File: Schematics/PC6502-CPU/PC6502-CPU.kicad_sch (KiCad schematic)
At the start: 62 parts, among them J1 BUS, J4 TEST, J5 Conn_02x05_Odd_Even, J6 Conn_02x02_Odd_Even, U2 AS6C4008-55PCN, U3 SST39SF010, U4 ATF1502AS, U5 W65C02, U6 74AHC244, U8 MCP130-450DI/TO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

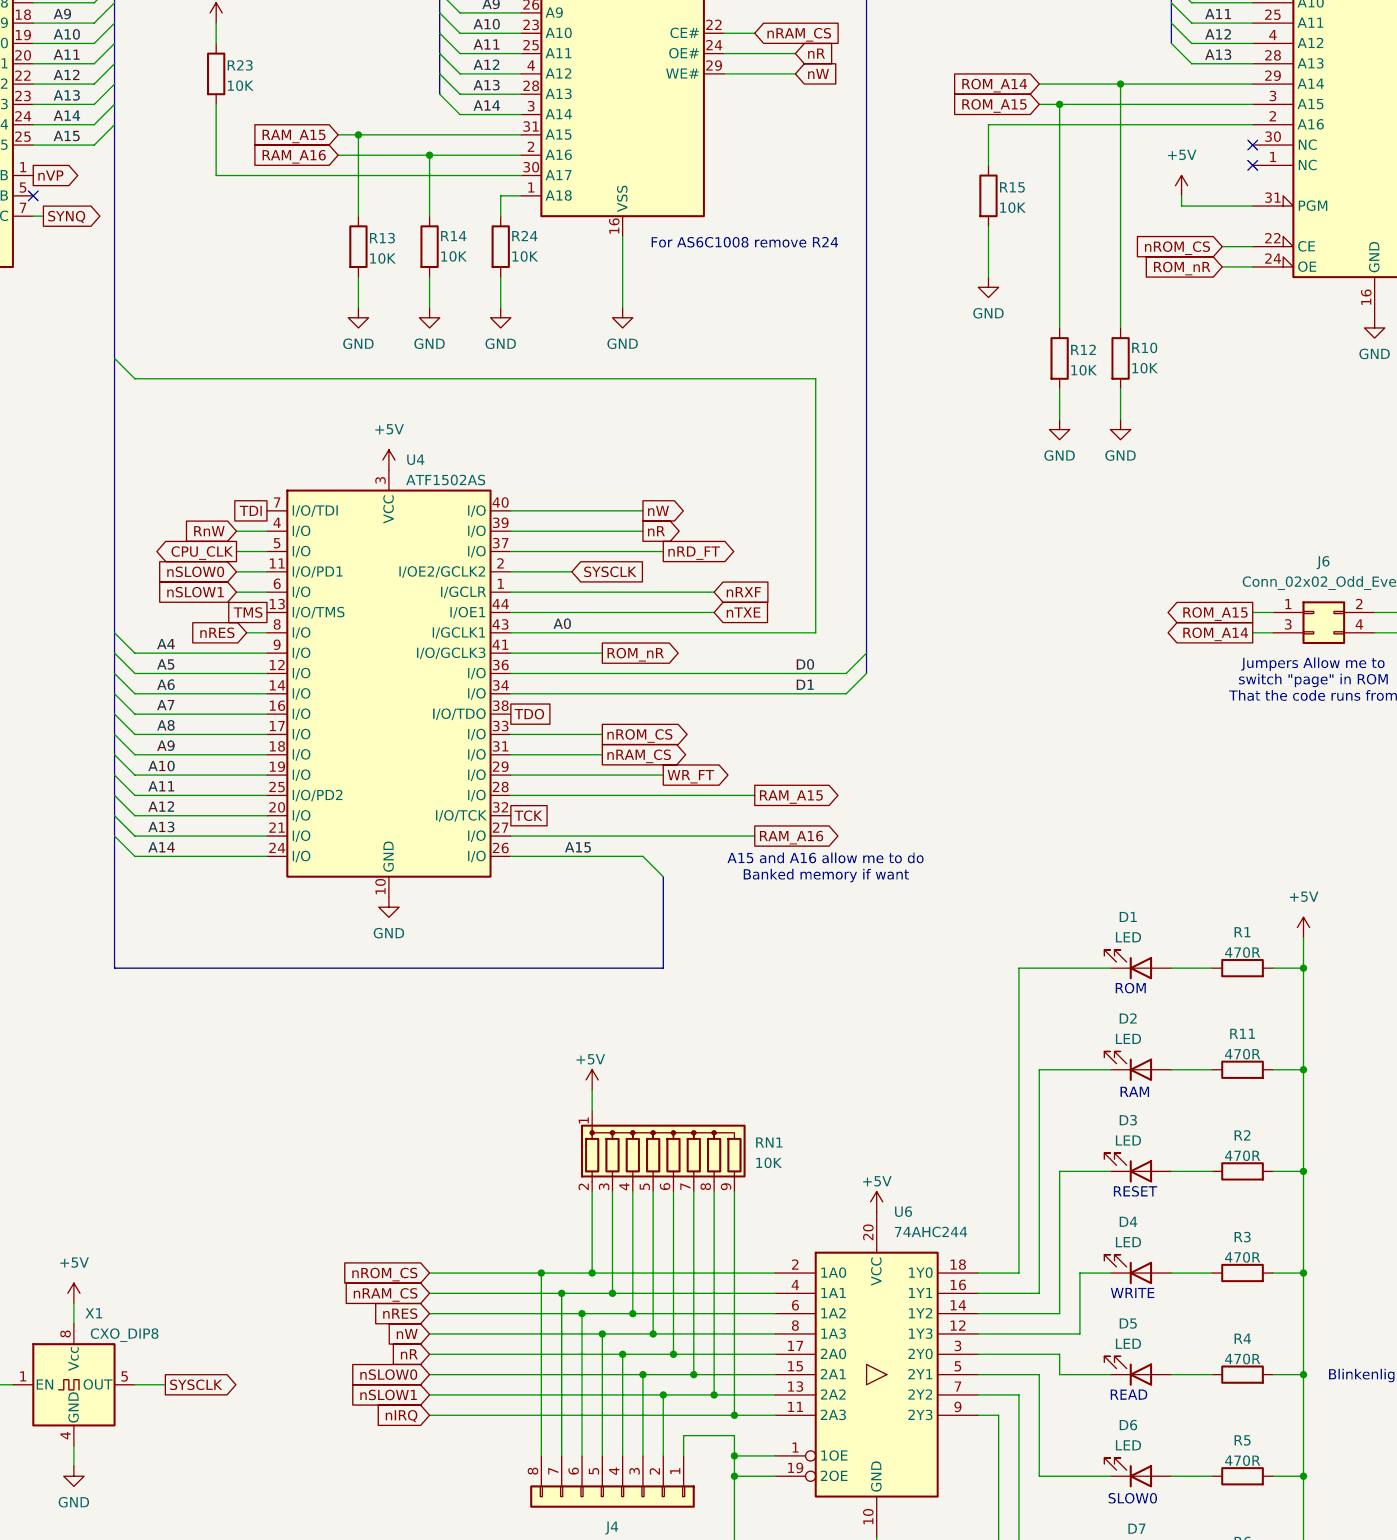
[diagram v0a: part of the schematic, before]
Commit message: Updated Schematics and CPLD files
Files updated for the CPU & FM Speech board
Also revised CPLDs for CPU, VIA and Compact Flasg
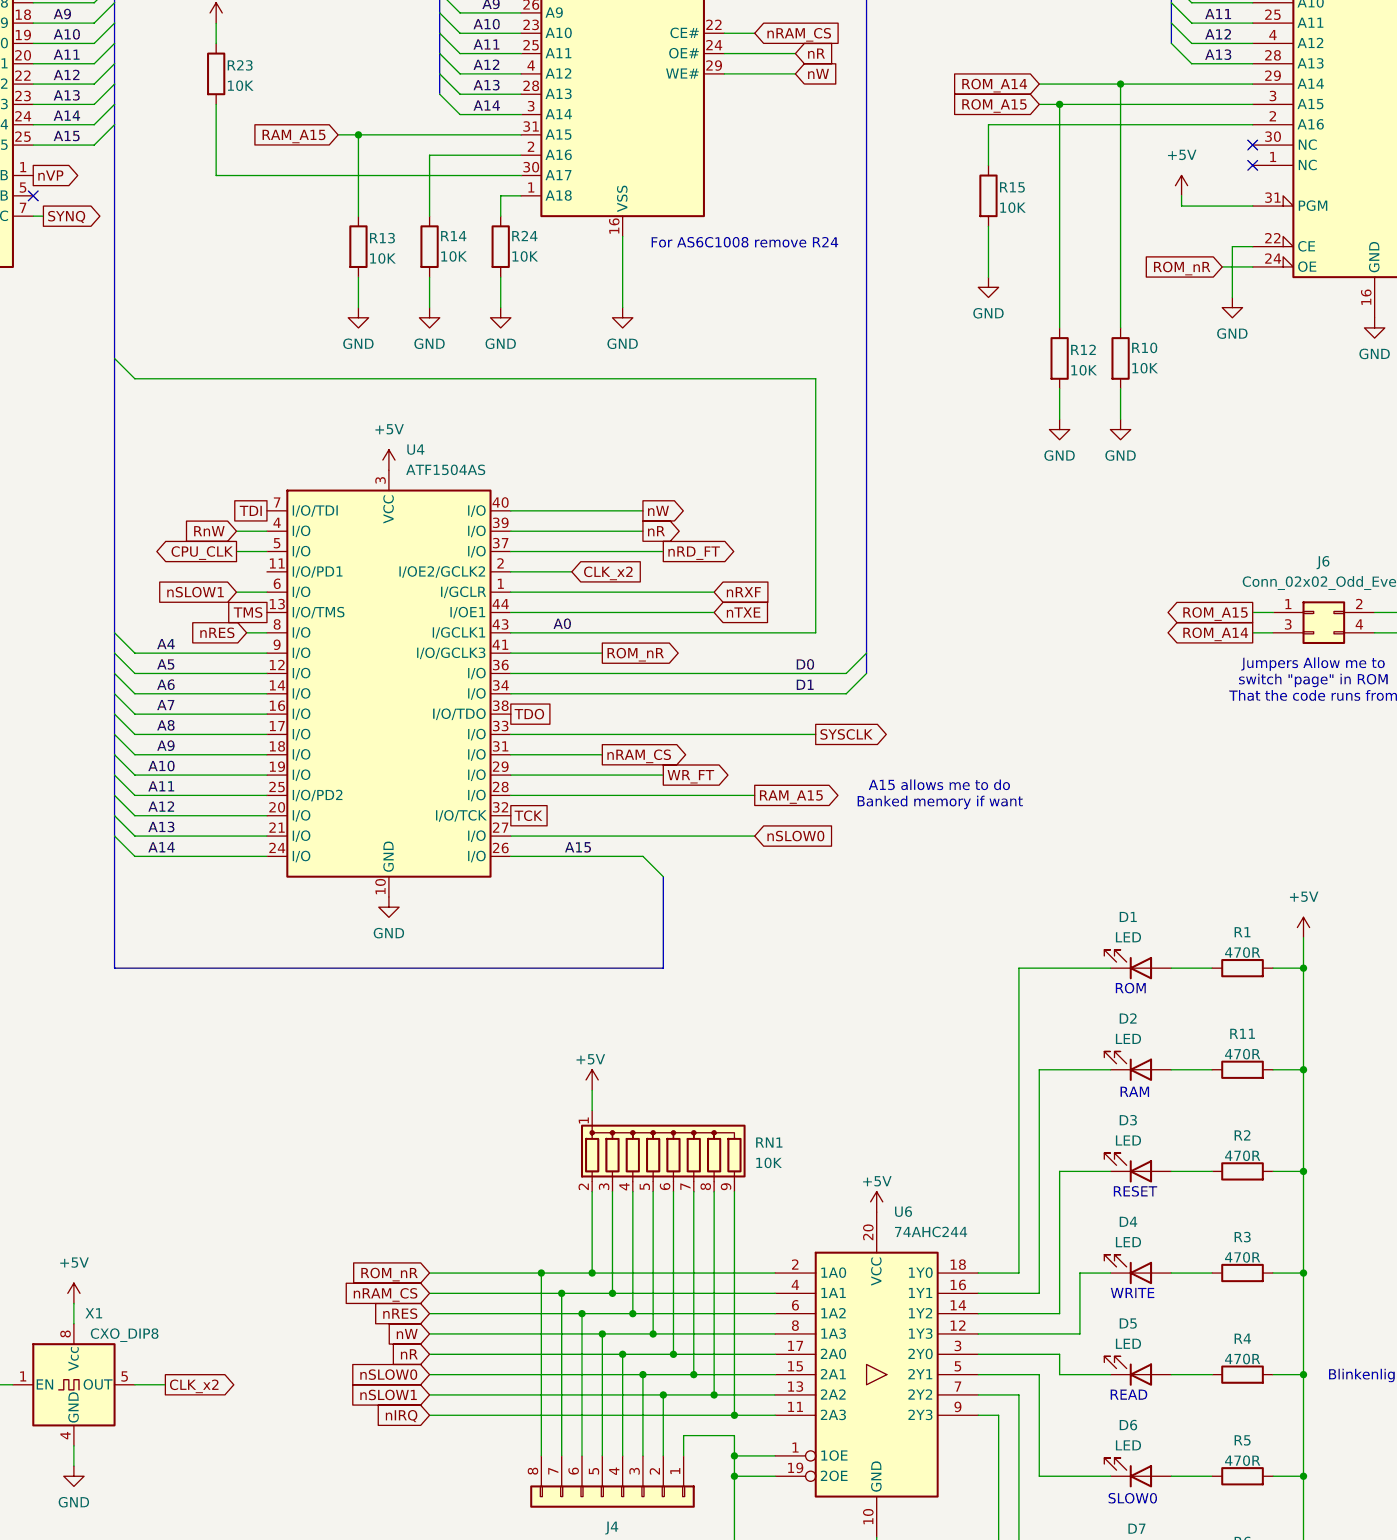
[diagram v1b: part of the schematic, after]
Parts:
- U4: value ATF1502AS -> ATF1504AS
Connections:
- net GND: now also U3.22 (CE)
- net ROM_nR: now also J4.8 (Pin_8), RN1.2 (R1), U6.2 (1A0)
- net SYSCLK: now also U4.33 (I/O); no longer U4.2 (I/OE2/GCLK2), X1.5 (OUT)
- net nSLOW0: now also U4.27 (I/O); no longer U4.11 (I/O/PD1)
- net RAM_A16: no longer names the net of R14.1, U2.2 (A16)
- net RAM_A16: no longer U4.27 (I/O)
- removed net nROM_CS: J4.8 (Pin_8), RN1.2 (R1), U3.22 (CE), U4.33 (I/O), U6.2 (1A0)
- new net CLK_x2: U4.2 (I/OE2/GCLK2), X1.5 (OUT)
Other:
- note added: "A15 allows me to do Banked memory if want"
- note removed: "A15 and A16 allow me to do Banked memory if want"
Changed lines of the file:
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@@
 		)
 	)
-	(text "A15 and A16 allow me to do\nBanked memory if want"
+	(text "A15 allows me to do\nBanked memory if want"
 		(exclude_from_sim no)
-		(at 210.82 171.704 0)
+		(at 225.044 162.56 0)
 		(effects
 			(font
@@
 	)
 	(junction
-		(at 161.29 82.55)
-		(diameter 0)
-		(color 0 0 0 0)
-	)
-	(junction
 		(at 358.14 170.18)
 		(diameter 0)
@@
 	(wire
 		(pts
-			(xy 266.7 209.55) (xy 270.51 209.55)
+			(xy 261.62 93.98) (xy 264.16 93.98)
 		)
 		(stroke
@@
 	(wire
 		(pts
-			(xy 190.5 132.08) (xy 171.45 132.08)
+			(xy 266.7 209.55) (xy 270.51 209.55)
 		)
 		(stroke
@@
 	(wire
 		(pts
-			(xy 149.86 82.55) (xy 161.29 82.55)
+			(xy 190.5 132.08) (xy 171.45 132.08)
 		)
 		(stroke
@@
 	(wire
 		(pts
+			(xy 261.62 100.33) (xy 261.62 93.98)
+		)
+		(stroke
+			(width 0)
+			(type default)
+		)
+	)
+	(wire
+		(pts
 			(xy 234.95 222.25) (xy 234.95 184.15)
 		)
@@
 	(wire
 		(pts
-			(xy 137.16 134.62) (xy 140.97 134.62)
-		)
-		(stroke
-			(width 0)
-			(type default)
-		)
-	)
-	(wire
-		(pts
 			(xy 171.45 144.78) (xy 182.88 144.78)
 		)
@@
 	(wire
 		(pts
-			(xy 171.45 154.94) (xy 182.88 154.94)
-		)
-		(stroke
-			(width 0)
-			(type default)
-		)
-	)
-	(wire
-		(pts
 			(xy 161.29 232.41) (xy 185.42 232.41)
 		)
@@
 	(wire
 		(pts
-			(xy 260.35 93.98) (xy 264.16 93.98)
+			(xy 171.45 154.94) (xy 209.55 154.94)
 		)
 		(stroke
@@
 		)
 	)
-	(global_label "SYSCLK"
-		(shape output)
-		(at 128.27 236.22 0)
+	(global_label "SYNQ"
+		(shape input)
+		(at 367.03 177.8 0)
 		(fields_autoplaced yes)
 		(effects
@@
 		)
 		(property "Intersheetrefs" "${INTERSHEET_REFS}"
-			(at 138.3309 236.22 0)
+			(at 374.9743 177.8 0)
 			(effects
 				(font
@@
 		)
 	)
-	(global_label "SYNQ"
-		(shape input)
-		(at 367.03 177.8 0)
+	(global_label "nVP"
+		(shape output)
+		(at 111.76 85.09 0)
 		(fields_autoplaced yes)
 		(effects
@@
 		)
 		(property "Intersheetrefs" "${INTERSHEET_REFS}"
-			(at 374.9743 177.8 0)
+			(at 118.2528 85.09 0)
 			(effects
 				(font
@@
 		)
 	)
-	(global_label "nVP"
-		(shape output)
-		(at 111.76 85.09 0)
+	(global_label "ROM_nR"
+		(shape input)
+		(at 161.29 222.25 180)
 		(fields_autoplaced yes)
 		(effects
@@
 				(size 1.27 1.27)
 			)
-			(justify left)
+			(justify right)
 		)
 		(property "Intersheetrefs" "${INTERSHEET_REFS}"
-			(at 118.2528 85.09 0)
+			(at 150.8663 222.25 0)
 			(effects
 				(font
 					(size 1.27 1.27)
 				)
-				(justify left)
+				(justify right)
 				(hide yes)
 			)
 		)
 	)
-	(global_label "RAM_A16"
+	(global_label "nRES"
 		(shape input)
-		(at 149.86 82.55 180)
+		(at 138.43 142.24 180)
 		(fields_autoplaced yes)
 		(effects
@@
 		)
 		(property "Intersheetrefs" "${INTERSHEET_REFS}"
-			(at 138.5896 82.55 0)
+			(at 130.6673 142.24 0)
 			(effects
 				(font
@@
 		)
 	)
-	(global_label "nRES"
-		(shape input)
-		(at 138.43 142.24 180)
+	(global_label "CLK_x2"
+		(shape output)
+		(at 128.27 236.22 0)
 		(fields_autoplaced yes)
 		(effects
@@
 				(size 1.27 1.27)
 			)
-			(justify right)
+			(justify left)
 		)
 		(property "Intersheetrefs" "${INTERSHEET_REFS}"
-			(at 130.6673 142.24 0)
+			(at 138.0285 236.22 0)
 			(effects
 				(font
 					(size 1.27 1.27)
 				)
-				(justify right)
+				(justify left)
 				(hide yes)
 			)
@@
 		)
 	)
-	(global_label "nROM_CS"
-		(shape input)
-		(at 260.35 93.98 180)
-		(fields_autoplaced yes)
-		(effects
-			(font
-				(size 1.27 1.27)
-			)
-			(justify right)
-		)
-		(property "Intersheetrefs" "${INTERSHEET_REFS}"
-			(at 248.7168 93.98 0)
-			(effects
-				(font
-					(size 1.27 1.27)
-				)
-				(justify right)
-				(hide yes)
-			)
-		)
-	)
 	(global_label "nRAM_CS"
 		(shape input)
@@
 	(global_label "nSLOW0"
 		(shape input)
-		(at 137.16 134.62 180)
+		(at 201.93 167.64 0)
 		(fields_autoplaced yes)
 		(effects
@@
 				(size 1.27 1.27)
 			)
-			(justify right)
+			(justify left)
 		)
 		(property "Intersheetrefs" "${INTERSHEET_REFS}"
-			(at 126.7968 134.62 0)
+			(at 212.2932 167.64 0)
 			(effects
 				(font
 					(size 1.27 1.27)
 				)
-				(justify right)
+				(justify left)
 				(hide yes)
 			)
@@
 		)
 	)
-	(global_label "nROM_CS"
-		(shape input)
-		(at 161.29 222.25 180)
-		(fields_autoplaced yes)
-		(effects
-			(font
-				(size 1.27 1.27)
-			)
-			(justify right)
-		)
-		(property "Intersheetrefs" "${INTERSHEET_REFS}"
-			(at 149.6568 222.25 0)
-			(effects
-				(font
-					(size 1.27 1.27)
-				)
-				(justify right)
-				(hide yes)
-			)
-		)
-	)
 	(global_label "nR"
 		(shape input)
@@
 		)
 	)
-	(global_label "nROM_CS"
-		(shape output)
-		(at 182.88 154.94 0)
-		(fields_autoplaced yes)
-		(effects
-			(font
-				(size 1.27 1.27)
-			)
-			(justify left)
-		)
-		(property "Intersheetrefs" "${INTERSHEET_REFS}"
-			(at 194.5132 154.94 0)
-			(effects
-				(font
-					(size 1.27 1.27)
-				)
-				(justify left)
-				(hide yes)
-			)
-		)
-	)
 	(global_label "nBUSRQ"
 		(shape input)
@@
 		)
 	)
-	(global_label "RAM_A16"
+	(global_label "SYNQ"
 		(shape output)
-		(at 201.93 167.64 0)
+		(at 113.03 90.17 0)
 		(fields_autoplaced yes)
 		(effects
@@
 		)
 		(property "Intersheetrefs" "${INTERSHEET_REFS}"
-			(at 213.2004 167.64 0)
+			(at 120.9743 90.17 0)
 			(effects
 				(font
@@
 		)
 	)
-	(global_label "SYNQ"
-		(shape output)
-		(at 113.03 90.17 0)
+	(global_label "nVP"
+		(shape input)
+		(at 335.28 187.96 180)
 		(fields_autoplaced yes)
 		(effects
@@
 				(size 1.27 1.27)
 			)
-			(justify left)
+			(justify right)
 		)
 		(property "Intersheetrefs" "${INTERSHEET_REFS}"
-			(at 120.9743 90.17 0)
+			(at 328.7872 187.96 0)
 			(effects
 				(font
 					(size 1.27 1.27)
 				)
-				(justify left)
+				(justify right)
 				(hide yes)
 			)
 		)
 	)
-	(global_label "nVP"
-		(shape input)
-		(at 335.28 187.96 180)
+	(global_label "SYSCLK"
+		(shape output)
+		(at 209.55 154.94 0)
 		(fields_autoplaced yes)
 		(effects
@@
 				(size 1.27 1.27)
 			)
-			(justify right)
+			(justify left)
 		)
 		(property "Intersheetrefs" "${INTERSHEET_REFS}"
-			(at 328.7872 187.96 0)
+			(at 219.6109 154.94 0)
 			(effects
 				(font
 					(size 1.27 1.27)
 				)
-				(justify right)
+				(justify left)
 				(hide yes)
 			)
@@
 		)
 	)
-	(global_label "SYSCLK"
+	(global_label "CLK_x2"
 		(shape input)
 		(at 179.07 134.62 0)
@@
 		)
 		(property "Intersheetrefs" "${INTERSHEET_REFS}"
-			(at 189.1309 134.62 0)
+			(at 188.8285 134.62 0)
 			(effects
 				(font
@@
 		(fields_autoplaced yes)
 		(property "Reference" "U4"
-			(at 158.3533 120.65 0)
+			(at 158.3533 119.38 0)
 			(effects
 				(font
@@
 			)
 		)
-		(property "Value" "ATF1502AS"
-			(at 158.3533 123.19 0)
+		(property "Value" "ATF1504AS"
+			(at 158.3533 121.92 0)
 			(effects
 				(font
@@
 					(unit 1)
 				)
+			)
+		)
+	)
+	(symbol
+		(lib_id "power:GND")
+		(at 261.62 100.33 0)
+		(unit 1)
+		(exclude_from_sim no)
+		(in_bom yes)
+		(on_board yes)
+		(dnp no)
+		(property "Reference" "#PWR052"
+			(at 261.62 106.68 0)
+			(effects
+				(font
+					(size 1.27 1.27)
+				)
+				(hide yes)
+			)
+		)
+		(property "Value" "GND"
+			(at 261.62 104.8925 0)
+			(effects
+				(font
+					(size 1.27 1.27)
+				)
+			)
+		)
+		(property "Footprint" ""
+			(at 261.62 100.33 0)
+			(effects
+				(font
+					(size 1.27 1.27)
+				)
+				(hide yes)
+			)
+		)
+		(property "Datasheet" ""
+			(at 261.62 100.33 0)
+			(effects
+				(font
+					(size 1.27 1.27)
+				)
+				(hide yes)
+			)
+		)
+		(property "Description" ""
+			(at 261.62 100.33 0)
+			(effects
+				(font
+					(size 1.27 1.27)
+				)
+			)
+		)
+		(pin "1"
+		)
+		(instances
+			(project "PC6502-CPU"
+				(path "/f3365b77-bdc1-4fa0-8030-841dab6ab2be"
+					(reference "#PWR052")
+					(unit 1)
+				)
